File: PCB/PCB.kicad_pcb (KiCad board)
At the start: 4 copper layers, 54 x 29 mm, 83 parts, among them J1 USB_B_Micro, Q1 PJA3428, Q2 PJA3428, Q3 AO3401A, Q4 BC546, SW1 SW_Push, SW2 SW_Push, SW3 SW_Push, SW4 ON/OFF, U1 ESP32-PICO-MINI-02, U2 CP2102N-Axx-xQFN24, U3 TP4056, U4 LM2578, U5 BNO080, Y1 32.768 kHz, Y2 32.768 kHz

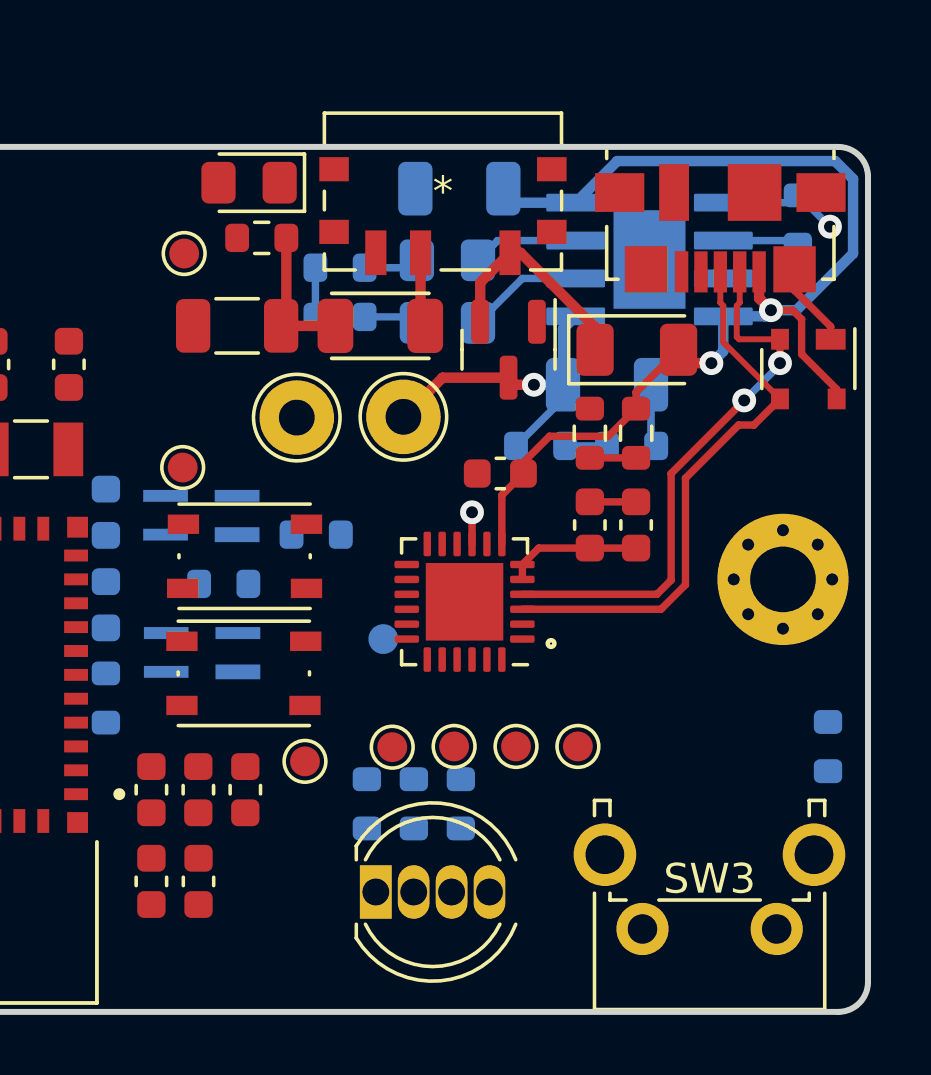
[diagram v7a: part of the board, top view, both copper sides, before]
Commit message: fix power plane issue and more routing
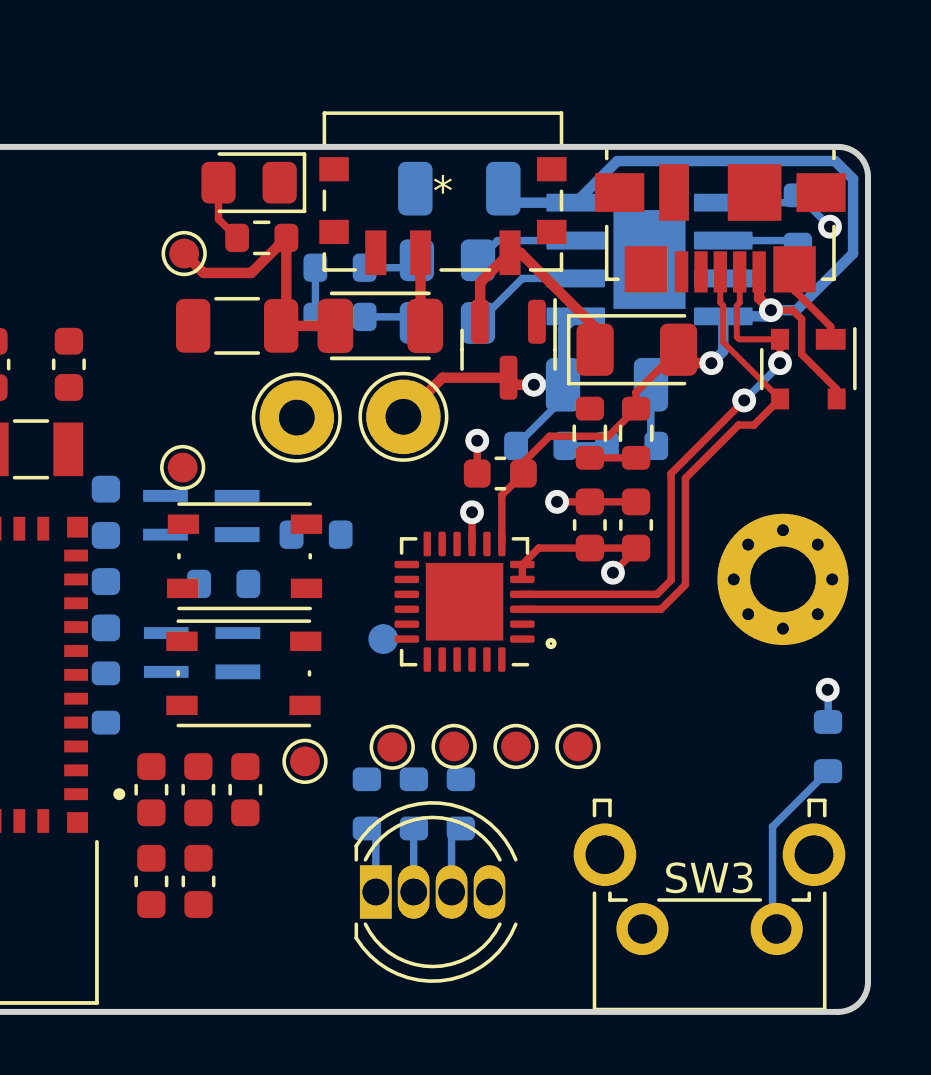
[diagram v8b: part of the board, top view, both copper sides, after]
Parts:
- turned R18 to 90 degrees
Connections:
- C1 pad 1: +3V3 -> +3.3V
- C10 pad 1: +3V3 -> +3.3V
- C3 pad 1: +3V3 -> +3.3V
- C4 pad 1: +3V3 -> +3.3V
- C5 pad 1: +3V3 -> +3.3V
- C6 pad 1: +3V3 -> +3.3V
- C9 pad 1: +3V3 -> +3.3V
- R21 pad 1: +3V3 -> +3.3V
- R22 pad 1: +3V3 -> +5V
- R23 pad 1: +3V3 -> +5V
- R24 pad 1: +3V3 -> +3.3V
- R25 pad 1: +3V3 -> +3.3V
- R4 pad 1: +3V3 -> +3.3V
- U1 pad 3: +3V3 -> +3.3V
- U2 pad 5: +3V3 -> +3.3V
- U2 pad 6: +3V3 -> +3.3V
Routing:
- net +3.3V: track 0.00 -> 6.77 mm, vias 0 -> 2
- net +3V3: track 7.25 -> 1.06 mm
- net SESSION_BUTTON: track 0.00 -> 6.12 mm
- net Vin: track 4.84 -> 9.02 mm
- net Net-(D6-Pad3): track 0.00 -> 2.26 mm
- net Net-(D6-Pad1): track 0.00 -> 2.25 mm
- net GND: track 10.6 -> 12.8 mm, vias 1 -> 3
- net Net-(D6-Pad2): track 0.00 -> 2.13 mm
- net Net-(D5-Pad2): track 0.00 -> 2.11 mm
- net +5V: track 39.4 -> 41.0 mm
